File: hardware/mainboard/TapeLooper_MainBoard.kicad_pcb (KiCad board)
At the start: 2 copper layers, 119.5 x 106.5 mm, 242 parts, among them J1 Micro_SD_Card, J10 VOL_B, J11 PITCH_C, J12 PITCH_D, J13 VOL_C, J14 VOL_D, J2 Conn_02x05_Odd_Even, J3 AUDIO_IN_L, J4 AUDIO_IN_R, J5 AUDIO_OUT_L, J6 AUDIO_OUT_R, J7 PITCH_A, J8 PITCH_B, J9 VOL_A, SW1 BTTN_LOAD, SW10 BTTN_PLAY_B, SW11 BTTN_PLAY_C, SW12 BTTN_PLAY_D, SW2 BTTN_DIRECTION, SW3 BTTN_SAVE, SW4 BTTN_REC, SW5 BTTN_SPEED_A, SW6 BTTN_SPEED_B, SW7 BTTN_SPEED_C, SW8 BTTN_SPEED_D, SW9 BTTN_PLAY_A, U1 DAISY_SEED, U10 AZ1117-2.5, U11 AZ1117-3.3, U2 EC4SAW-24S05N, U3 AZ1117-5.0, U4 TL074, U5 PCA9685PW, U6 PCA9685PW, U7 PCA9685PW, U8 MAX11300_TQFP, U9 MAX11300_TQFP

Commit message: hardware: update schematics & add BOM
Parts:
- D10: value LED_DIRECTION -> LED_RED_GREEN_CA
- D11: value LED_REC -> LED_RED_GREEN_CA
- D12: value LED_SPEED_+2_A -> LED_RED_GREEN_CA
- D13: value LED_SPEED_+2_C -> LED_RED_GREEN_CA
- D14: value LED_SPEED_+1_A -> LED_RED_GREEN_CA
- D15: value LED_SPEED_+1_C -> LED_RED_GREEN_CA
- D16: value LED_SPEED_-1_A -> LED_RED_GREEN_CA
- D17: value LED_SPEED_-1_C -> LED_RED_GREEN_CA
- D18: value LED_SPEED_-2_A -> LED_RED_GREEN_CA
- D19: value LED_SPEED_-2_C -> LED_RED_GREEN_CA
- D20: value LED_SPEED_+2_B -> LED_RED_GREEN_CA
- D21: value LED_SPEED_+2_D -> LED_RED_GREEN_CA
- D22: value LED_SPEED_+1_B -> LED_RED_GREEN_CA
- D23: value LED_SPEED_+1_D -> LED_RED_GREEN_CA
- D24: value LED_SPEED_-1_B -> LED_RED_GREEN_CA
- D25: value LED_SPEED_-1_D -> LED_RED_GREEN_CA
- D26: value LED_SPEED_-2_B -> LED_RED_GREEN_CA
- D27: value LED_SPEED_-2_D -> LED_RED_GREEN_CA
- D4: value LED_IN_L -> LED_RED_GREEN_CA
- D5: value LED_IN_R -> LED_RED_GREEN_CA
- D6: value LED_OUT_L -> LED_RED_GREEN_CA
- D7: value LED_OUT_R -> LED_RED_GREEN_CA
- D8: value LED_LOAD -> LED_RED_GREEN_CA
- D9: value LED_SAVE -> LED_RED_GREEN_CA
- J10: value VOL_B -> PJ398SM
- J11: value PITCH_C -> PJ398SM
- J12: value PITCH_D -> PJ398SM
- J13: value VOL_C -> PJ398SM
- J14: value VOL_D -> PJ398SM
- J3: value AUDIO_IN_L -> PJ398SM
- J4: value AUDIO_IN_R -> PJ398SM
- J5: value AUDIO_OUT_L -> PJ398SM
- J6: value AUDIO_OUT_R -> PJ398SM
- J7: value PITCH_A -> PJ398SM
- J8: value PITCH_B -> PJ398SM
- J9: value VOL_A -> PJ398SM
- R21, R22, R23, R26, R27, R28, R29, R30, R31, R32, R33, R34, R35, R36, R37, R38, R39, R40, R41, R42, R43, R44, R45, R46, R47, R48, R49, R50, R51, R52, R53, R54, R55, R56, R57, R58, R59, R60, R61, R62, R63, R64, R65, R66, R67, R68, R69, R70: value Rled -> 330
- SW1: value BTTN_LOAD -> TL1105SPF250Q
- SW10: value BTTN_PLAY_B -> D6R90F1LFS
- SW11: value BTTN_PLAY_C -> D6R90F1LFS
- SW12: value BTTN_PLAY_D -> D6R90F1LFS
- SW2: value BTTN_DIRECTION -> TL1105SPF250Q
- SW3: value BTTN_SAVE -> TL1105SPF250Q
- SW4: value BTTN_REC -> D6R40F1LFS
- SW5: value BTTN_SPEED_A -> C&K 7105SYCQE
- SW6: value BTTN_SPEED_B -> C&K 7105SYCQE
- SW7: value BTTN_SPEED_C -> C&K 7105SYCQE
- SW8: value BTTN_SPEED_D -> C&K 7105SYCQE
- SW9: value BTTN_PLAY_A -> D6R90F1LFS
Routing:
- net SPI_CS_AB: track 57.1 -> 56.1 mm

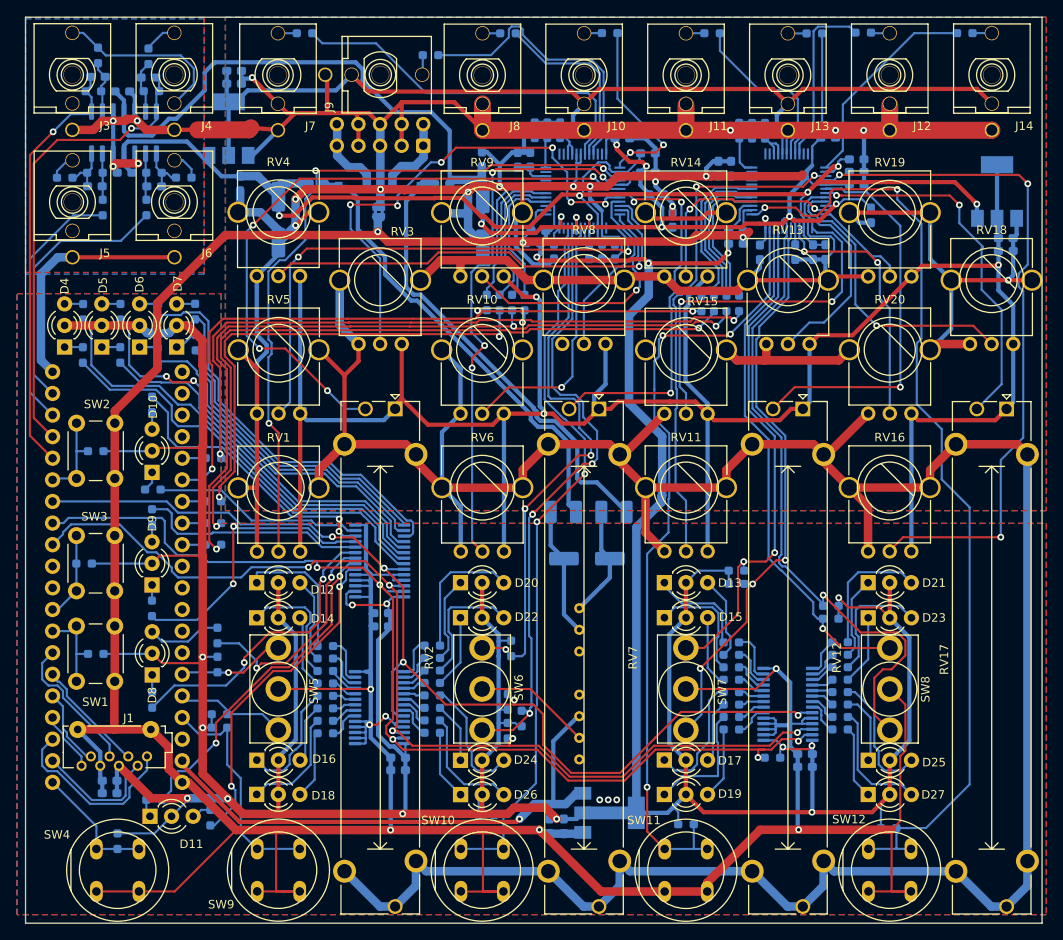
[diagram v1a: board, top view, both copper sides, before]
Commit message: hardware: swap MAX11300 for ordinary multiplexers; PCB v1.1
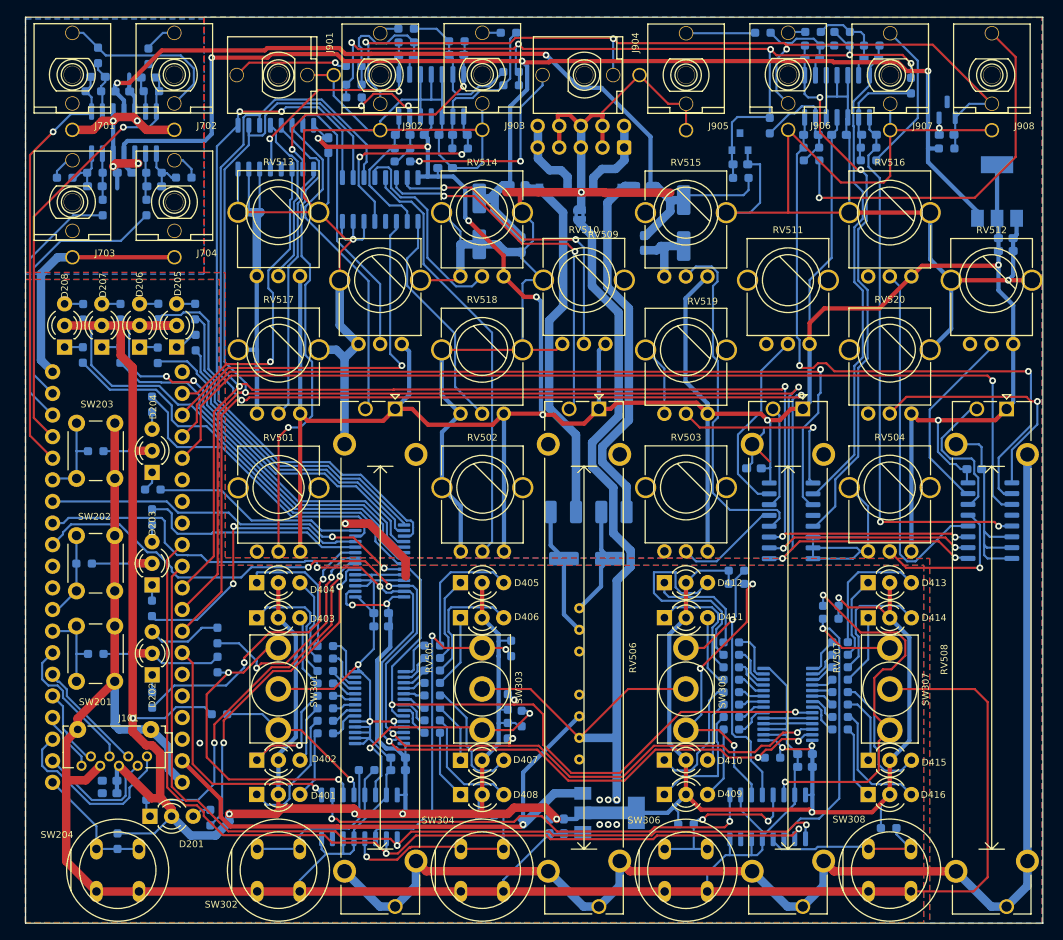
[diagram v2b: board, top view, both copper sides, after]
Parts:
- removed C19, C20, C33, C37, C38, C48: 10u, Capacitor_SMD:C_0603_1608Metric_Pad1.08x0.95mm_HandSolder
- removed C21, C22, C23, C25, C26, C27, C31, C32, C34, C35, C36, C39, C40, C41, C42, C45, C46, C47, C49, C51, C52, C53, C55: 100n, Capacitor_SMD:C_0603_1608Metric_Pad1.08x0.95mm_HandSolder
- removed C24, C30, C50, C54, C56: 4u7, Capacitor_SMD:C_0603_1608Metric_Pad1.08x0.95mm_HandSolder
- removed J10, J11, J12, J13, J14, J7, J8, J9: PJ398SM, ell_connectors:THONKICONN
- removed R1, R2, R3, R4, R83, R84, R85, R86, R91, R92, R93, R94: 20R, Resistor_SMD:R_0603_1608Metric_Pad0.98x0.95mm_HandSolder
- removed R87, R88, R89, R90, R95, R96, R97, R98: 1k, Resistor_SMD:R_0603_1608Metric_Pad0.98x0.95mm_HandSolder
- removed U3: AZ1117-5.0, Package_TO_SOT_SMD:SOT-223-3_TabPin2
- removed U8, U9: MAX11300_TQFP, Package_QFP:TQFP-48_7x7mm_P0.5mm
- added C601: 100n, Capacitor_SMD:C_0603_1608Metric_Pad1.08x0.95mm_HandSolder, B.Cu at (119.1, 58.7)
- added C602: 100n, Capacitor_SMD:C_0603_1608Metric_Pad1.08x0.95mm_HandSolder, B.Cu at (132.8, 61.4)
- added C603: 100n, Capacitor_SMD:C_0603_1608Metric_Pad1.08x0.95mm_HandSolder, B.Cu at (169.1, 96.7)
- added C604: 100n, Capacitor_SMD:C_0603_1608Metric_Pad1.08x0.95mm_HandSolder, B.Cu at (195.0, 96.8)
- added C801: 4u7, Capacitor_SMD:C_0603_1608Metric_Pad1.08x0.95mm_HandSolder, B.Cu at (191.8, 57.5)
- added C806: 4u7, Capacitor_SMD:C_0603_1608Metric_Pad1.08x0.95mm_HandSolder, B.Cu at (167.5, 61.0)
- added C901: 1n, Capacitor_SMD:C_0603_1608Metric_Pad1.08x0.95mm_HandSolder, B.Cu at (128.2, 48.2)
- added C902: 1n, Capacitor_SMD:C_0603_1608Metric_Pad1.08x0.95mm_HandSolder, B.Cu at (134.2, 48.1)
- added C903: 100n, Capacitor_SMD:C_0603_1608Metric_Pad1.08x0.95mm_HandSolder, B.Cu at (131.2, 57.5)
- added C904: 1n, Capacitor_SMD:C_0603_1608Metric_Pad1.08x0.95mm_HandSolder, B.Cu at (134.6, 57.5)
- added C905: 1n, Capacitor_SMD:C_0603_1608Metric_Pad1.08x0.95mm_HandSolder, B.Cu at (127.8, 57.5)
- added C906: 1n, Capacitor_SMD:C_0603_1608Metric_Pad1.08x0.95mm_HandSolder, B.Cu at (176.0, 48.5)
- added C907: 1n, Capacitor_SMD:C_0603_1608Metric_Pad1.08x0.95mm_HandSolder, B.Cu at (182.9, 48.5)
- added C908: 100n, Capacitor_SMD:C_0603_1608Metric_Pad1.08x0.95mm_HandSolder, B.Cu at (179.1, 57.5)
- added C909: 1n, Capacitor_SMD:C_0603_1608Metric_Pad1.08x0.95mm_HandSolder, B.Cu at (182.7, 57.5)
- added C910: 1n, Capacitor_SMD:C_0603_1608Metric_Pad1.08x0.95mm_HandSolder, B.Cu at (175.8, 57.5)
- added J901: PJ398SM, ell_connectors:THONKICONN, F.Cu at (113.3, 50.5)
- added J902: PJ398SM, ell_connectors:THONKICONN, F.Cu at (125.2, 50.5)
- added J903: PJ398SM, ell_connectors:THONKICONN, F.Cu at (137.2, 50.4)
- added J904: PJ398SM, ell_connectors:THONKICONN, F.Cu at (149.2, 50.5)
- added J905: PJ398SM, ell_connectors:THONKICONN, F.Cu at (161.2, 50.5)
- added J906: PJ398SM, ell_connectors:THONKICONN, F.Cu at (173.2, 50.4)
- added J907: PJ398SM, ell_connectors:THONKICONN, F.Cu at (185.2, 50.5)
- added J908: PJ398SM, ell_connectors:THONKICONN, F.Cu at (197.1, 50.5)
- added R801: 2k2, Resistor_SMD:R_0603_1608Metric_Pad0.98x0.95mm_HandSolder, B.Cu at (191.8, 59.1)
- added R802: 2k2, Resistor_SMD:R_0603_1608Metric_Pad0.98x0.95mm_HandSolder, B.Cu at (167.6, 62.6)
- added R901: 100k, Resistor_SMD:R_0603_1608Metric_Pad0.98x0.95mm_HandSolder, B.Cu at (122.1, 49.4)
- added R902: 78k7, Resistor_SMD:R_0603_1608Metric_Pad0.98x0.95mm_HandSolder, B.Cu at (128.3, 46.6)
- added R903: 100k, Resistor_SMD:R_0603_1608Metric_Pad0.98x0.95mm_HandSolder, B.Cu at (128.3, 45.0)
- added R904: 68k, Resistor_SMD:R_0603_1608Metric_Pad0.98x0.95mm_HandSolder, B.Cu at (134.2, 46.5)
- added R905: 480k, Resistor_SMD:R_0603_1608Metric_Pad0.98x0.95mm_HandSolder, B.Cu at (122.1, 51.6)
- added R906: 200k, Resistor_SMD:R_0603_1608Metric_Pad0.98x0.95mm_HandSolder, B.Cu at (140.6, 50.1)
- added R907: 100k, Resistor_SMD:R_0603_1608Metric_Pad0.98x0.95mm_HandSolder, B.Cu at (140.3, 45.5)
- added R908: 78k7, Resistor_SMD:R_0603_1608Metric_Pad0.98x0.95mm_HandSolder, B.Cu at (134.6, 59.1)
- added R909: 100k, Resistor_SMD:R_0603_1608Metric_Pad0.98x0.95mm_HandSolder, B.Cu at (127.8, 60.6)
- added R910: 68k, Resistor_SMD:R_0603_1608Metric_Pad0.98x0.95mm_HandSolder, B.Cu at (127.8, 59.1)
- added R911: 480k, Resistor_SMD:R_0603_1608Metric_Pad0.98x0.95mm_HandSolder, B.Cu at (140.6, 51.7)
- added R912: 200k, Resistor_SMD:R_0603_1608Metric_Pad0.98x0.95mm_HandSolder, B.Cu at (122.1, 53.1)
- added R913: 100k, Resistor_SMD:R_0603_1608Metric_Pad0.98x0.95mm_HandSolder, B.Cu at (170.2, 45.5)
- added R914: 78k7, Resistor_SMD:R_0603_1608Metric_Pad0.98x0.95mm_HandSolder, B.Cu at (176.1, 47.0)
- added R915: 100k, Resistor_SMD:R_0603_1608Metric_Pad0.98x0.95mm_HandSolder, B.Cu at (176.1, 45.4)
- added R916: 68k, Resistor_SMD:R_0603_1608Metric_Pad0.98x0.95mm_HandSolder, B.Cu at (183.0, 47.0)
- added R917: 480k, Resistor_SMD:R_0603_1608Metric_Pad0.98x0.95mm_HandSolder, B.Cu at (179.5, 47.0)
- added R918: 200k, Resistor_SMD:R_0603_1608Metric_Pad0.98x0.95mm_HandSolder, B.Cu at (179.5, 45.4)
- added R919: 100k, Resistor_SMD:R_0603_1608Metric_Pad0.98x0.95mm_HandSolder, B.Cu at (182.6, 60.5)
- added R920: 78k7, Resistor_SMD:R_0603_1608Metric_Pad0.98x0.95mm_HandSolder, B.Cu at (182.6, 59.0)
- added R921: 100k, Resistor_SMD:R_0603_1608Metric_Pad0.98x0.95mm_HandSolder, B.Cu at (175.9, 60.5)
- added R922: 68k, Resistor_SMD:R_0603_1608Metric_Pad0.98x0.95mm_HandSolder, B.Cu at (175.9, 59.0)
- added R923: 480k, Resistor_SMD:R_0603_1608Metric_Pad0.98x0.95mm_HandSolder, B.Cu at (187.6, 51.7)
- added R924: 200k, Resistor_SMD:R_0603_1608Metric_Pad0.98x0.95mm_HandSolder, B.Cu at (171.0, 56.4)
- added U601: 4051, Package_SO:SO-16_3.9x9.9mm_P1.27mm, B.Cu at (112.9, 58.9)
- added U602: 4051, Package_SO:SO-16_3.9x9.9mm_P1.27mm, B.Cu at (125.2, 65.1)
- added U603: 4051, Package_SO:SO-16_3.9x9.9mm_P1.27mm, B.Cu at (173.5, 102.9)
- added U604: 4051, Package_SO:SO-16_3.9x9.9mm_P1.27mm, B.Cu at (196.9, 102.8)
- added U605: 74HC165, Package_SO:SO-16_3.9x9.9mm_P1.27mm, B.Cu at (170.8, 137.7)
- added U606: 74HC165, Package_SO:SO-16_3.9x9.9mm_P1.27mm, B.Cu at (122.8, 137.7)
- added U801: LM4040DBZ-5, Package_TO_SOT_SMD:SOT-23, B.Cu at (191.8, 54.6)
- added U803: LM4040DBZ-10, Package_TO_SOT_SMD:SOT-23, B.Cu at (167.5, 58.3)
- added U901: MCP6004, Package_SO:SO-14_3.9x8.65mm_P1.27mm, B.Cu at (131.2, 52.9)
- added U902: MCP6004, Package_SO:SO-14_3.9x8.65mm_P1.27mm, B.Cu at (178.9, 53.0)
- R702: renamed from R14; value 24k -> 10k
- R704: renamed from R15; value 24k -> 10k
- R706: renamed from R6; value 24k -> 10k
- R709: renamed from R7; value 24k -> 10k
- U802: renamed from U10; value AZ1117-2.5 -> AZ1117-3.3
- moved C803 33.8 mm to (141.8, 70.4)
- moved JP801 23.6 mm to (148.6, 66.9)
- moved C802 23.6 mm to (136.8, 67.7)
- moved L801 23.6 mm to (141.4, 63.4)
- moved C807 23.6 mm to (160.9, 67.9)
- moved D801 23.6 mm to (145.6, 63.8)
- moved D802 23.6 mm to (151.9, 63.8)
- moved J801 23.6 mm to (153.9, 59.0)
- moved L802 23.6 mm to (156.1, 63.5)
- moved C808 21.4 mm to (156.2, 70.2), turned to 90 degrees
- moved R303 18.0 mm to (123.6, 132.2)
- renumbered C1 to C101, C2 to C102, C13 to C201, C14 to C202, C15 to C401, C17 to C402, C16 to C403, C18 to C404, C59 to C701, C11 to C702, C60 to C703, C12 to C704, C57 to C705, C58 to C706, C4 to C802, C6 to C803, C8 to C804, C9 to C805, C5 to C807, C7 to C808, C3 to C809, C61 to C810, C62 to C811, D11 to D201, D8 to D202, D9 to D203, D10 to D204, D7 to D205, D6 to D206, D5 to D207, D4 to D208, D18 to D401, D16 to D402, D14 to D403, D12 to D404, D20 to D405, D22 to D406, D24 to D407, D26 to D408, D19 to D409, D17 to D410, D15 to D411, D13 to D412, D21 to D413, D23 to D414, D25 to D415, D27 to D416, D1 to D801, D2 to D802, J1 to J101, J3 to J701, J4 to J702, J5 to J703, J6 to J704, J2 to J801, JP1 to JP801, L1 to L801, L2 to L802, L3 to L803, L4 to L804, R37 to R201, R38 to R202, R31 to R203, R32 to R204, R33 to R205, R34 to R206, R35 to R207, R36 to R208, R29 to R209, R30 to R210, R27 to R211, R28 to R212, R23 to R213, R26 to R214, R21 to R215, R22 to R216, R16 to R217, R17 to R218, R18 to R219, R19 to R220, R24 to R221, R20 to R222, R25 to R223, R71 to R301, R75 to R302, R79 to R303, R72 to R304, R76 to R305, R80 to R306, R73 to R307, R77 to R308, R81 to R309, R74 to R310, R78 to R311, R82 to R312, R39 to R401, R41 to R402, R43 to R403, R45 to R404, R47 to R405, R49 to R406, R51 to R407, R53 to R408, R55 to R409, R57 to R410, R59 to R411, R61 to R412, R63 to R413, R65 to R414, R67 to R415, R69 to R416, R40 to R417, R42 to R418, R44 to R419, R46 to R420, R48 to R421, R50 to R422, R52 to R423, R54 to R424, R56 to R425, R58 to R426, R60 to R427, R62 to R428, R64 to R429, R66 to R430, R68 to R431, R70 to R432, R10 to R701, R11 to R703, R12 to R705, R8 to R707, R13 to R708, R9 to R710, RV1 to RV501, RV6 to RV502, RV11 to RV503, RV16 to RV504, RV2 to RV505, RV7 to RV506, RV12 to RV507, RV17 to RV508, RV3 to RV509, RV8 to RV510, RV13 to RV511, RV18 to RV512, RV4 to RV513, RV9 to RV514, RV14 to RV515, RV19 to RV516, RV5 to RV517, RV10 to RV518, RV15 to RV519, RV20 to RV520, SW1 to SW201, SW3 to SW202, SW2 to SW203, SW4 to SW204, SW5 to SW301, SW9 to SW302, SW6 to SW303, SW10 to SW304, SW7 to SW305, SW11 to SW306, SW8 to SW307, SW12 to SW308, U1 to U101, U5 to U201, U6 to U401, U7 to U402, U4 to U701, U11 to U804, U2 to U805
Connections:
- net +2V5 renamed +3.3VA
- net BTTN_DIRECTION renamed BTTN_SETTINGS
- J701 pad 2: (no net) -> unconnected-(J701-TN-Pad2)
- J703 pad 2: (no net) -> unconnected-(J703-TN-Pad2)
- J704 pad 2: (no net) -> unconnected-(J704-TN-Pad2)
- U101 pad 10: (no net) -> unconnected-(U101-D9/PB4/UART7_TX/SPI1,3,6_MISO/I2S1,3_SDI/I2S2_WS/TIM3_1-Pad10)
- U101 pad 11: (no net) -> unconnected-(U101-D10/PB5/UART5_RS/SPI1,3,6_MOSI/I2S1,3_SDO/TIM3_2/HRTIM_EEV7-Pad11)
- U101 pad 21: (no net) -> unconnected-(U101-3V3A-Pad21)
- U101 pad 22: (no net) -> ADC_A
- U101 pad 23: (no net) -> ADC_B
- U101 pad 24: (no net) -> ADC_C
- U101 pad 25: Net-(R2-Pad1) -> ADC_D
- U101 pad 26: SPI_MISO -> unconnected-(U101-A4/D19/PA6/ADC12_3/SPI1,6,_MISO/I2S1_SDI/TIM3,13_1-Pad26)
- U101 pad 27: Net-(R3-Pad1) -> unconnected-(U101-A5/D20/PC1/ADC123_11/SPI2_MOSI/I2S2_SDO/SAI1_D1-Pad27)
- U101 pad 28: Net-(R1-Pad1) -> unconnected-(U101-A6/D21/PC4/ADC12_4/I2S1_MCK-Pad28)
- U101 pad 29: Net-(R4-Pad1) -> SR_CLK
- U101 pad 30: (no net) -> SR_NLOAD
- U101 pad 31: (no net) -> MUX_A
- U101 pad 32: (no net) -> MUX_B
- U101 pad 33: (no net) -> MUX_C
- U101 pad 34: (no net) -> SR_MISO
- U101 pad 35: BTTN_DOWN_A -> unconnected-(U101-A11/D28/PA2/ADC12_14/SAI2_SCK_B/USART2_TX/TIM2,5_3/TIM15_1-Pad35)
- U101 pad 36: BTTN_UP_A -> unconnected-(U101-D29/PB14/USB_D-/USART1_TX/SPI2_MISO/I2S2_SDI/TIM12_1-Pad36)
- U101 pad 37: BTTN_PLAY_A -> unconnected-(U101-D30/PB15/USB_D+/USART1_RX/SPI2_MOSI/I2S2_SDO/RTC_REFIN/TIM12_2-Pad37)
- U101 pad 38: (no net) -> unconnected-(U101-3V3D-Pad38)
- U805 pad 3: (no net) -> unconnected-(U805-On/Off-Pad3)
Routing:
- net MUX_C: track 0.00 -> 197.0 mm, vias 0 -> 6
- net MUX_B: track 0.00 -> 194.9 mm, vias 0 -> 4
- net MUX_A: track 0.00 -> 189.2 mm, vias 0 -> 4
- net GNDA: track 926.8 -> 784.9 mm, vias 19 -> 8
- net ADC_D: track 0.00 -> 118.0 mm, vias 0 -> 1
- net SR_CLK: track 0.00 -> 111.7 mm, vias 0 -> 2
- net SR_NLOAD: track 0.00 -> 107.9 mm, vias 0 -> 2
- net -10V: track 0.00 -> 103.9 mm, vias 0 -> 5
- net +3V3: track 532.4 -> 434.0 mm, vias 15 -> 11
- net ADC_C: track 0.00 -> 96.9 mm, vias 0 -> 1
- net BTTN_PLAY_D: track 112.0 -> 20.2 mm, vias 2 -> 0
- net +3.3VA: track 275.5 -> 367.2 mm, vias 3 -> 8
- net SPI_SCLK: track 91.4 -> 0.00 mm, vias 3 -> 0
- net -12VA: track 189.5 -> 98.1 mm, vias 10 -> 2
- net SPI_CS_CD: track 83.8 -> 0.00 mm, vias 2 -> 0
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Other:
- board size 119.5 x 106.5 mm -> 119.6 x 106.5 mm
- net class Default removed
- board text added: "Johannes Elliesen 2024"
- board text added: "v1.1"
- board text removed: "Johannes Elliesen 2021"

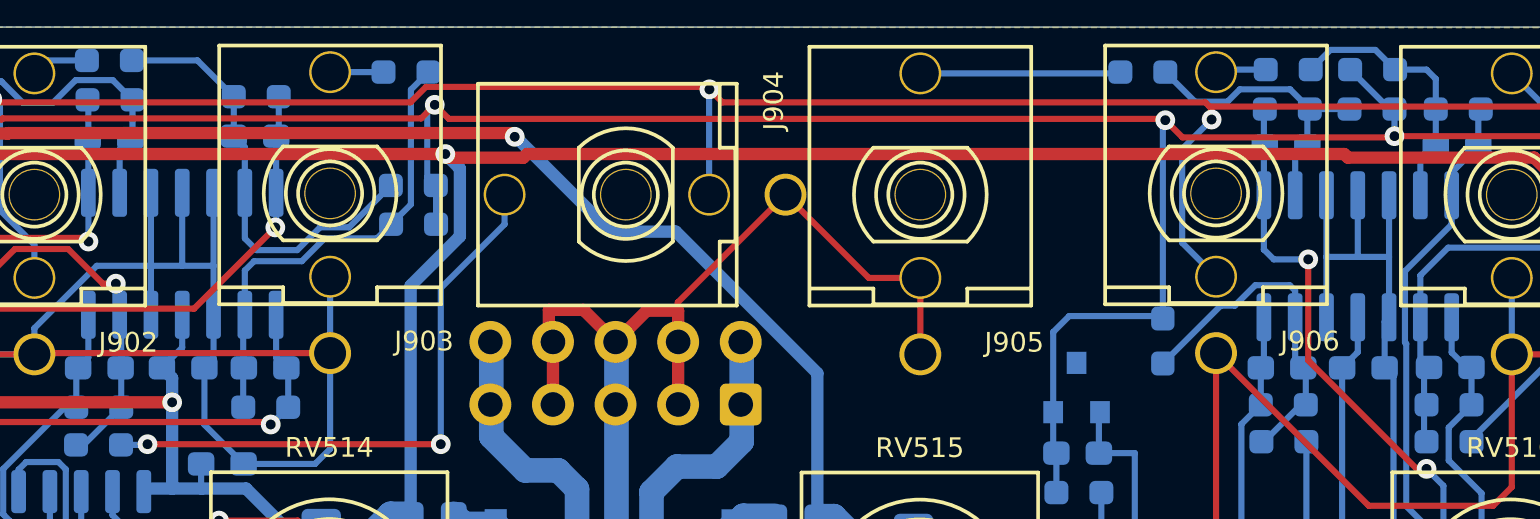
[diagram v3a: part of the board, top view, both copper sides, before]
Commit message: hardware: fix reverse MCP6004 power pins
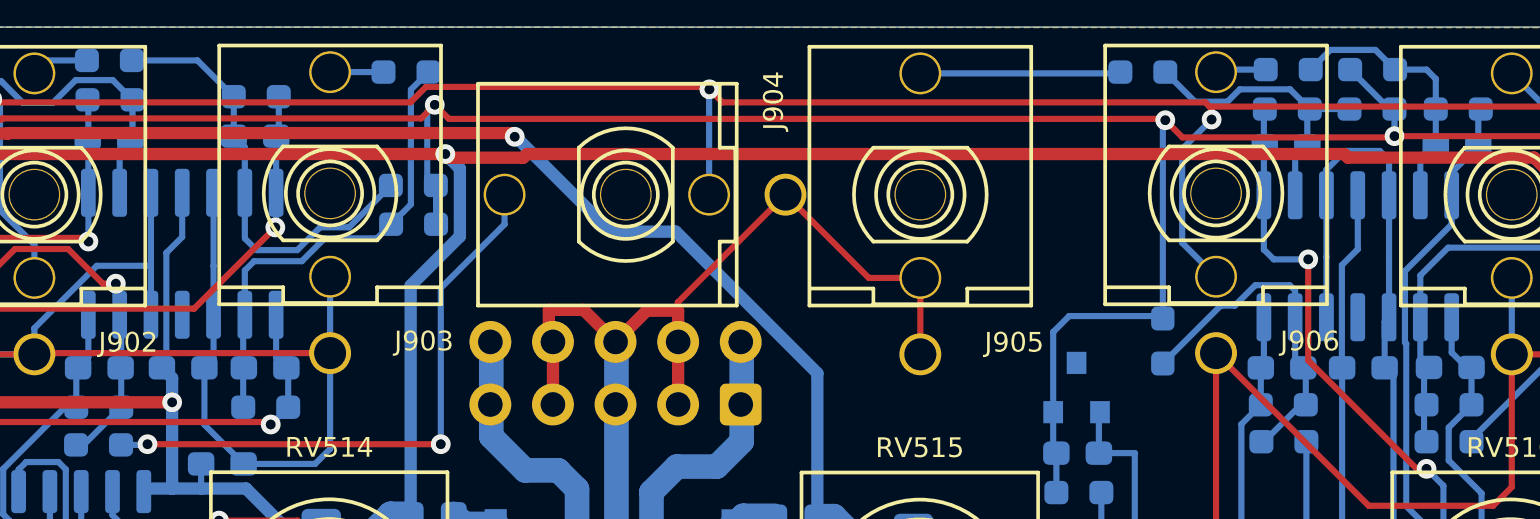
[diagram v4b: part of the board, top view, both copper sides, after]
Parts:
- R702, R704, R706, R709: value 10k -> 8k2
- R905, R911, R917, R923: value 480k -> 481k
- SW204: value D6R40F1LFS -> D6R40F1LFS
- SW302, SW304, SW306, SW308: value D6R90F1LFS -> D6R90F1LFS
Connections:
- U901 pad 11: +3.3VA -> GNDA
- U901 pad 4: GNDA -> +3.3VA
- U902 pad 11: +3.3VA -> GNDA
- U902 pad 4: GNDA -> +3.3VA
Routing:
- net +3.3VA: track 367.2 -> 377.1 mm
- net GNDA: track 784.9 -> 779.9 mm

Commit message: hardware: add missing SD card pullups
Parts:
- added R101: 47k, Resistor_SMD:R_0603_1608Metric_Pad0.98x0.95mm_HandSolder, B.Cu at (94.3, 136.5)
- added R102: 47k, Resistor_SMD:R_0603_1608Metric_Pad0.98x0.95mm_HandSolder, B.Cu at (93.4, 138.6)
- added R103: 47k, Resistor_SMD:R_0603_1608Metric_Pad0.98x0.95mm_HandSolder, B.Cu at (90.9, 136.5)
- added R104: 47k, Resistor_SMD:R_0603_1608Metric_Pad0.98x0.95mm_HandSolder, B.Cu at (91.0, 135.0)
- added R105: 47k, Resistor_SMD:R_0603_1608Metric_Pad0.98x0.95mm_HandSolder, B.Cu at (92.6, 128.4)
- added R106: 47k, Resistor_SMD:R_0603_1608Metric_Pad0.98x0.95mm_HandSolder, B.Cu at (92.6, 126.9)
- moved C102 0.91 mm to (94.3, 133.5)
- moved C101 0.91 mm to (94.3, 135.0)
- moved R223 0.86 mm to (94.3, 141.4)
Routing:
- net +3V3: track 434.0 -> 450.6 mm, vias 11 -> 15
- net Net-(J101-DAT2): track 21.7 -> 29.4 mm
- net Net-(J101-DAT3/CD): track 14.8 -> 22.0 mm
- net Net-(J101-DAT0): track 9.25 -> 15.2 mm
- net Net-(J101-DAT1): track 7.08 -> 12.9 mm
- net Net-(J101-CMD): track 13.5 -> 15.9 mm
- net Net-(J101-CLK): track 16.6 -> 18.9 mm
- net BTTN_REC: track 15.0 -> 16.3 mm
- net GND: track 506.1 -> 505.4 mm
